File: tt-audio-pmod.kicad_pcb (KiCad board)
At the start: 2 copper layers, 41.1 x 27.9 mm, 18 parts, among them J1 10129382-912001BLF, J2 Female header, J5 PJ-320B, U1 74LVCE1G126SE-7

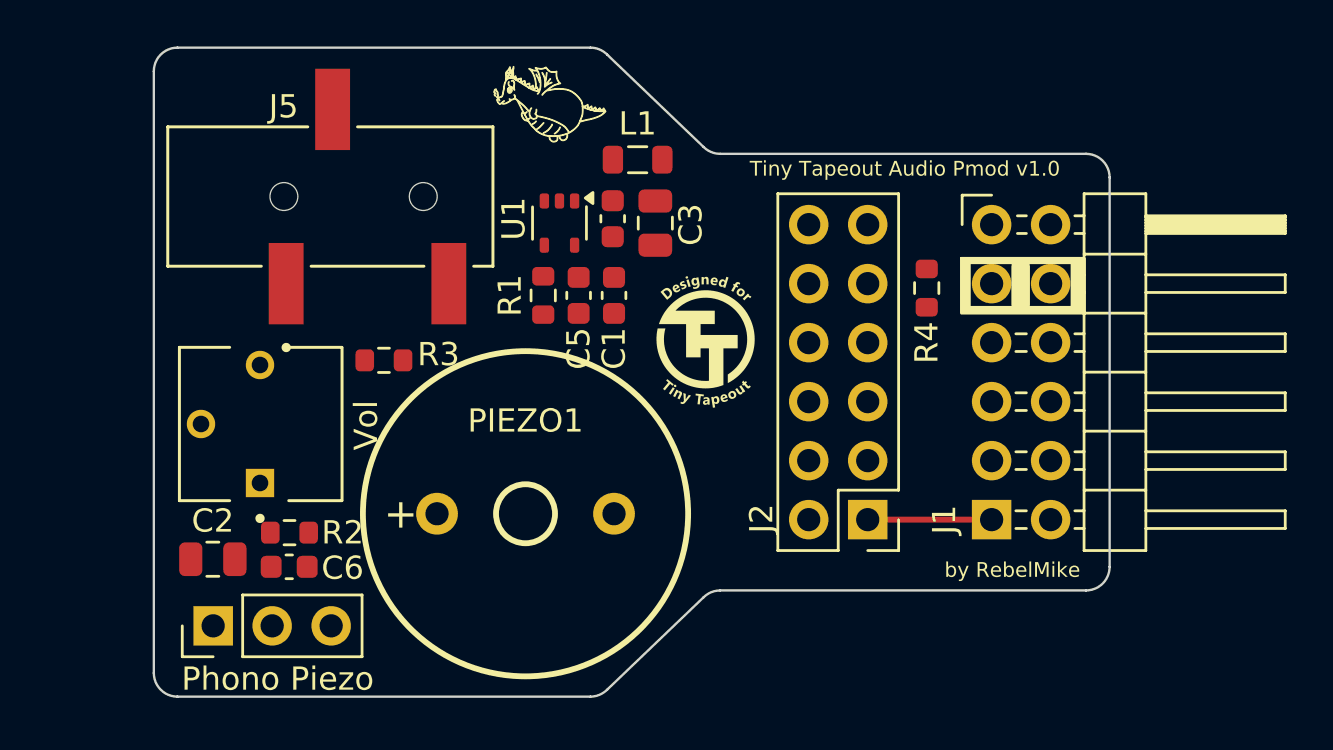
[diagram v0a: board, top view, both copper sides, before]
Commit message: Change board shape
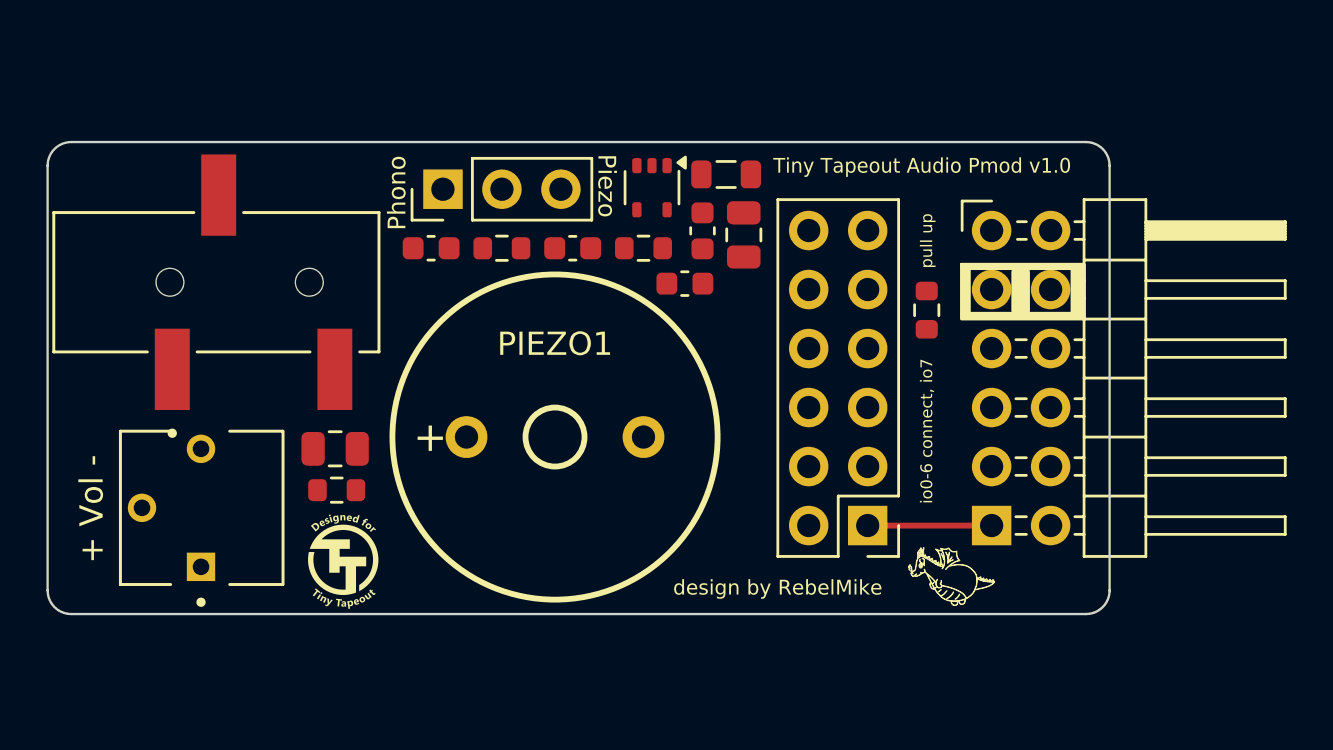
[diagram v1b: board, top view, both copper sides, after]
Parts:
- + Vol -: renamed from Vol
- moved Phono Piezo 21.2 mm to (90.2, 35.1)
- moved R2 15.3 mm to (92.7, 37.6)
- moved C6 15.0 mm to (89.7, 37.6), turned to 180 degrees
- moved C2 7.09 mm to (85.5, 46.2), turned to 0 degrees
- moved J5 6.14 mm to (81.4, 39.1)
- moved R3 5.95 mm to (85.6, 48.0), turned to 0 degrees
- moved R1 4.77 mm to (98.8, 37.6), turned to 0 degrees
- moved + Vol - 4.41 mm to (79.8, 48.8)
- moved U1 4.27 mm to (99.2, 35.0)
- moved C4 3.90 mm to (101.3, 36.8)
- moved L1 3.86 mm to (102.4, 34.4)
- moved C3 3.84 mm to (103.1, 37.0)
- moved PIEZO1 3.54 mm to (95.0, 45.7)
- moved C1 3.09 mm to (100.6, 39.1), turned to 0 degrees
- moved C5 2.05 mm to (95.8, 37.6), turned to 0 degrees
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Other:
- board size 41.1 x 27.9 mm -> 45.7 x 20.3 mm
- board text added: "Phono"
- board text added: "Piezo"
- board text added: "design by RebelMike"
- board text added: "io0‐6 connect, io7"
- board text added: "pull up"
- board text removed: "by RebelMike"

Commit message: Minor tweaks
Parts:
- moved R4 1.91 mm to (111.0, 42.2)
- moved + Vol - 0.55 mm to (79.2, 48.8)
- moved C2 0.55 mm to (85.0, 46.2)
- moved R3 0.55 mm to (85.0, 48.0)
- moved PIEZO1 0.51 mm to (94.5, 45.7)
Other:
- board text added: "io0‐6 connect"
- board text added: "io7 pull up"
- board text removed: "io0‐6 connect, io7"
- board text removed: "pull up"

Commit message: Routed
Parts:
- J4: renamed from Phono Piezo
- RV1: renamed from + Vol -
- moved R4 0.27 mm to (111.0, 41.9)
- moved U1 0.25 mm to (99.2, 35.2)
- moved C1 0.13 mm to (100.6, 39.2)
- moved C3 0.13 mm to (103.1, 37.1)
- moved C4 0.13 mm to (101.3, 37.0)
- moved L1 0.13 mm to (102.4, 34.5)
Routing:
- net Net-(J4-Pin_1): track 0.00 -> 31.5 mm
- net pwm: track 0.00 -> 27.9 mm
- net 3V3: track 0.00 -> 16.5 mm
- net Net-(J4-Pin_3): track 0.00 -> 12.6 mm
- net io6: track 0.00 -> 11.4 mm
- net io5: track 0.00 -> 11.4 mm
- net io4: track 0.00 -> 11.4 mm
- net GND: track 0.00 -> 7.87 mm, vias 0 -> 11
- net Net-(U1-VCC): track 0.00 -> 6.88 mm
- net Net-(J2-Pin_10): track 0.00 -> 5.72 mm
- net io3: track 0.00 -> 5.33 mm
- net io2: track 0.00 -> 5.33 mm
- net io1: track 0.00 -> 5.33 mm
- net Net-(R1-Pad2): track 0.00 -> 1.86 mm
- net Net-(J4-Pin_2): track 0.00 -> 0.72 mm
- added copper zone on F.Cu, net 3V3
- added copper zone on B.Cu, net GND
- added copper zone on F.Cu, net GND
- added copper zone on F.Cu, net Net-(C1-Pad1)
- added copper zone on F.Cu, net Net-(C2-Pad1)
- added copper zone on F.Cu, net Net-(J4-Pin_2)
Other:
- board text added: "+ Vol -"

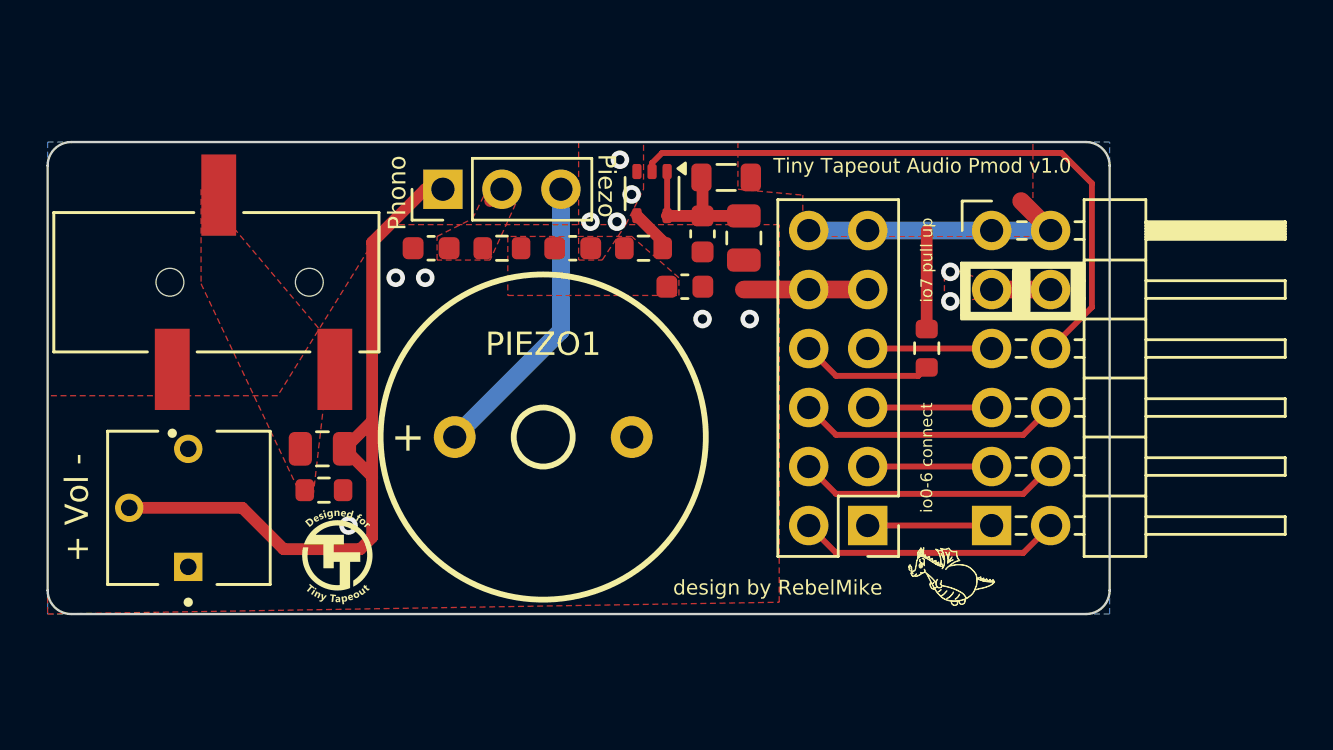
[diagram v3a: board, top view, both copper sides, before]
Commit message: Improve ground coherence and thermal relief
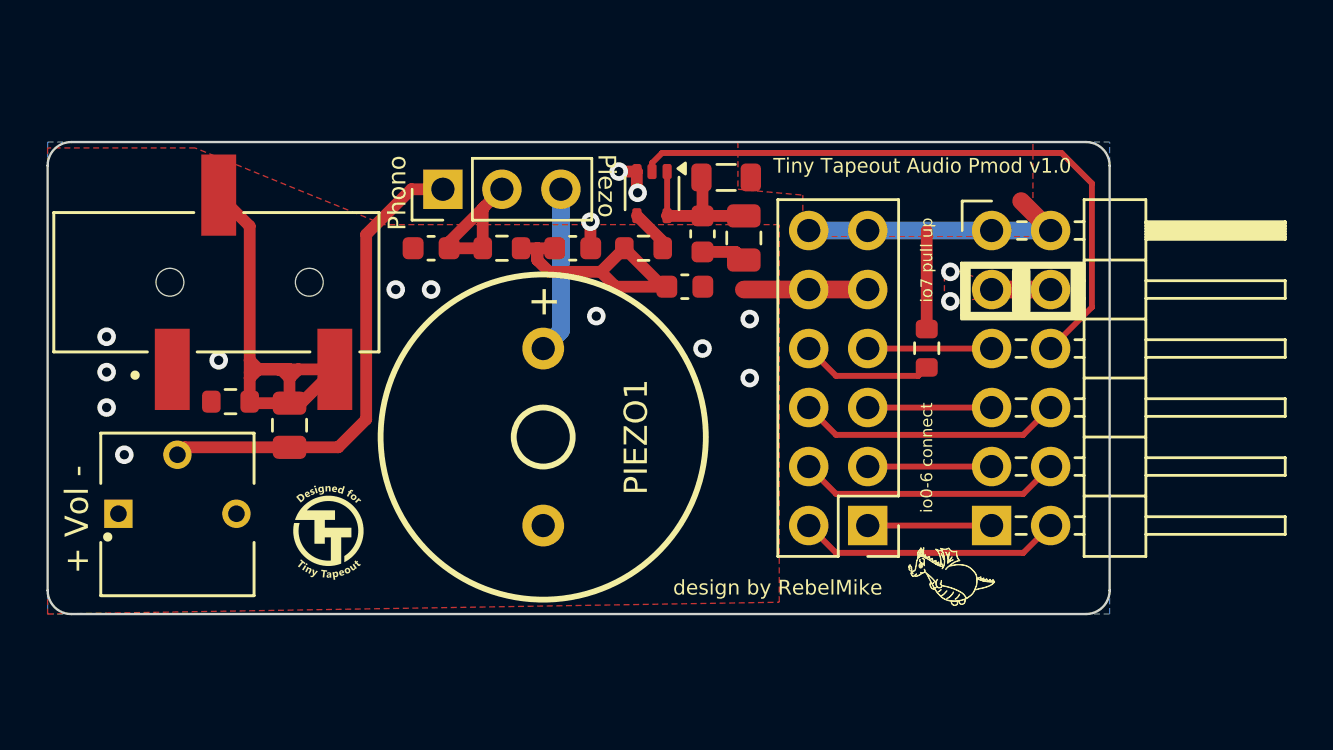
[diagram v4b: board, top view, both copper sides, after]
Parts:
- moved R3 5.54 mm to (81.0, 44.2), turned to 180 degrees
- moved C2 1.74 mm to (83.6, 45.2), turned to -90 degrees
- moved RV1 0.53 mm to (78.7, 49.0), turned to 0 degrees
- turned PIEZO1 to -90 degrees
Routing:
- net Net-(C2-Pad1): track 0.00 -> 22.1 mm
- net Net-(C1-Pad1): track 0.00 -> 12.2 mm
- net Net-(J4-Pin_1): track 31.5 -> 20.9 mm
- net Net-(J4-Pin_2): track 0.72 -> 6.73 mm
- net Net-(J4-Pin_3): track 12.6 -> 7.17 mm
- net GND: track 7.87 -> 12.7 mm, vias 11 -> 16
- removed copper zone on F.Cu, net Net-(C1-Pad1)
- removed copper zone on F.Cu, net Net-(C2-Pad1)
- removed copper zone on F.Cu, net Net-(J4-Pin_2)
